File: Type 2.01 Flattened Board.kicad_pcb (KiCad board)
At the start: 4 copper layers, 170 x 170 mm, 74 parts, among them J1 Conn_02x03_Odd_Even, J4 Conn_02x03_Odd_Even, J5 Conn_02x03_Odd_Even, U1 74AHC74, U10 74AHC74, U11 74AHC157, U12 74AHC157, U13 74AHC04, U14 ATmega4809-PF, U15 74AHC04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

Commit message: More pcb layout changes
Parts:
- removed C33, C34: 0.1uF, Capacitor_SMD:C_0805_2012Metric_Pad1.18x1.45mm_HandSolder
- removed U12, U22: 74AHC157, Package_SO:SOIC-16_3.9x9.9mm_P1.27mm
- U11, U2, U6: value 74AHC157 -> 74AHC245; footprint Package_SO:SOIC-16_3.9x9.9mm_P1.27mm -> Package_SO:SOIC-20W_7.5x12.8mm_P1.27mm
- U3: value 74AHC157 -> 74AHC138
- moved C37 108.1 mm to (89.9, 116.7), turned to 90 degrees
- moved U5 99.8 mm to (82.1, 112.6), turned to -90 degrees
- moved C15 97.4 mm to (104.7, 120.6), turned to 0 degrees
- moved C19 88.5 mm to (196.0, 47.9), turned to 180 degrees
- moved U4 83.1 mm to (191.9, 55.7), turned to 0 degrees
- moved U11 80.4 mm to (108.7, 112.8), turned to 180 degrees
- moved C5 67.9 mm to (133.5, 125.7), turned to 90 degrees
- moved C4 48.4 mm to (63.8, 98.1)
- moved C3 42.5 mm to (114.7, 78.0), turned to 90 degrees
- moved C2 40.7 mm to (162.6, 81.5)
- moved U17 38.9 mm to (127.1, 123.9), turned to -90 degrees
- moved U2 28.7 mm to (158.5, 89.3)
- moved U6 23.1 mm to (145.3, 76.3), turned to 90 degrees
- moved U3 19.0 mm to (108.3, 76.2), turned to -90 degrees
- moved C14 11.5 mm to (137.5, 72.2), turned to -90 degrees
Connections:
- U11 pad 1: /i960/SEL0 -> VCC
- U11 pad 10: /i960.A26 -> GND
- U11 pad 11: /i960.A10 -> /GCM4.L7
- U11 pad 12: /i960/Q11 -> /GCM4.L6
- U11 pad 13: /i960.A27 -> /GCM4.L5
- U11 pad 14: /i960.A11 -> /GCM4.L4
- U11 pad 15: GND -> /GCM4.L3
- U11 pad 16: VCC -> /GCM4.L2
- U11 pad 2: /i960.A8 -> /i960.DT\~{R}
- U11 pad 3: /i960.A24 -> /i960.BURST_A1
- U11 pad 4: /i960/Q8 -> /i960.BURST_A2
- U11 pad 5: /i960.A9 -> /i960.BURST_A3
- U11 pad 6: /i960.A25 -> /i960.~{BE0}
- U11 pad 7: /i960/Q9 -> /i960.~{BE1}
- U11 pad 8: GND -> /i960/CTRL07/IN6
- U11 pad 9: /i960/Q10 -> /i960/CTRL07/IN7
- U18 pad 1: /i960/i960.~{DEV_EN0} -> /i960/i960.~{DEV_EN1}
- U18 pad 12: /i960.A15 -> /GCM4.L7
- U18 pad 13: /i960.A14 -> /GCM4.L6
- U18 pad 14: /i960.A13 -> /GCM4.L5
- U18 pad 15: /i960.A12 -> /GCM4.L4
- U18 pad 16: /i960.A11 -> /GCM4.L3
- U18 pad 17: /i960.A10 -> /GCM4.L2
- U18 pad 18: /i960.A9 -> /GCM4.L1
- U18 pad 19: /i960.A8 -> /GCM4.L0
- U19 pad 12: /i960.A7 -> /GCM4.L7
- U19 pad 13: /i960.A6 -> /GCM4.L6
- U19 pad 14: /i960.A5 -> /GCM4.L5
- U19 pad 15: /i960.A4 -> /GCM4.L4
- U19 pad 16: /i960.A3 -> /GCM4.L3
- U19 pad 17: /i960.A2 -> /GCM4.L2
- U19 pad 18: /i960.A1 -> /GCM4.L1
- U19 pad 19: /i960.A0 -> /GCM4.L0
- U2 pad 1: /i960/SEL0 -> VCC
- U2 pad 10: /i960.A22 -> GND
- U2 pad 11: /i960.A6 -> /GCM4.L7
- U2 pad 12: /i960/Q7 -> /GCM4.L6
- U2 pad 13: /i960.A23 -> /GCM4.L5
- U2 pad 14: /i960.A7 -> /GCM4.L4
- U2 pad 15: GND -> /GCM4.L3
- U2 pad 16: VCC -> /GCM4.L2
- U2 pad 2: /i960.A4 -> /i960.A24
- U2 pad 3: /i960.A20 -> /i960.A25
- U2 pad 4: /i960/Q5 -> /i960.A26
- U2 pad 5: /i960.A5 -> /i960.A27
- U2 pad 6: /i960.A21 -> /i960.A28
- U2 pad 7: /i960/Q6 -> /i960.A29
- U2 pad 8: GND -> /i960.A30
- U2 pad 9: /i960/Q4 -> /i960.A31
- U3 pad 1: /i960/SEL0 -> /i960/GCM4.LA0
- U3 pad 10: /i960.A18 -> /i960/i960.~{DEV_EN5}
- U3 pad 11: /i960.A2 -> /i960/i960.~{DEV_EN4}
- U3 pad 12: /i960/Q3 -> /i960/i960.~{DEV_EN3}
- U3 pad 13: /i960.A19 -> /i960/i960.~{DEV_EN2}
- U3 pad 14: /i960.A3 -> /i960/i960.~{DEV_EN1}
- U3 pad 15: GND -> /i960/i960.~{DEV_EN0}
- U3 pad 2: /i960.A0 -> /i960/GCM4.LA1
- U3 pad 3: /i960.A16 -> /i960/GCM4.LA2
- U3 pad 4: /i960/Q0 -> /i960/GCM4.~{EN}
- U3 pad 5: /i960.A1 -> GND
- U3 pad 6: /i960.A17 -> VCC
- U3 pad 7: /i960/Q1 -> /i960/i960.~{DEV_EN7}
- U3 pad 9: /i960/Q2 -> /i960/i960.~{DEV_EN6}
- U6 pad 1: /i960/SEL0 -> VCC
- U6 pad 10: /i960.A30 -> GND
- U6 pad 11: /i960.A14 -> /GCM4.L7
- U6 pad 12: /i960/Q15 -> /GCM4.L6
- U6 pad 13: /i960.A31 -> /GCM4.L5
- U6 pad 14: /i960.A15 -> /GCM4.L4
- U6 pad 15: GND -> /GCM4.L3
- U6 pad 16: VCC -> /GCM4.L2
- U6 pad 2: /i960.A12 -> /i960.A16
- U6 pad 3: /i960.A28 -> /i960.A17
- U6 pad 4: /i960/Q13 -> /i960.A18
- U6 pad 5: /i960.A13 -> /i960.A19
- U6 pad 6: /i960.A29 -> /i960.A20
- U6 pad 7: /i960/Q14 -> /i960.A21
- U6 pad 8: GND -> /i960.A22
- U6 pad 9: /i960/Q12 -> /i960.A23

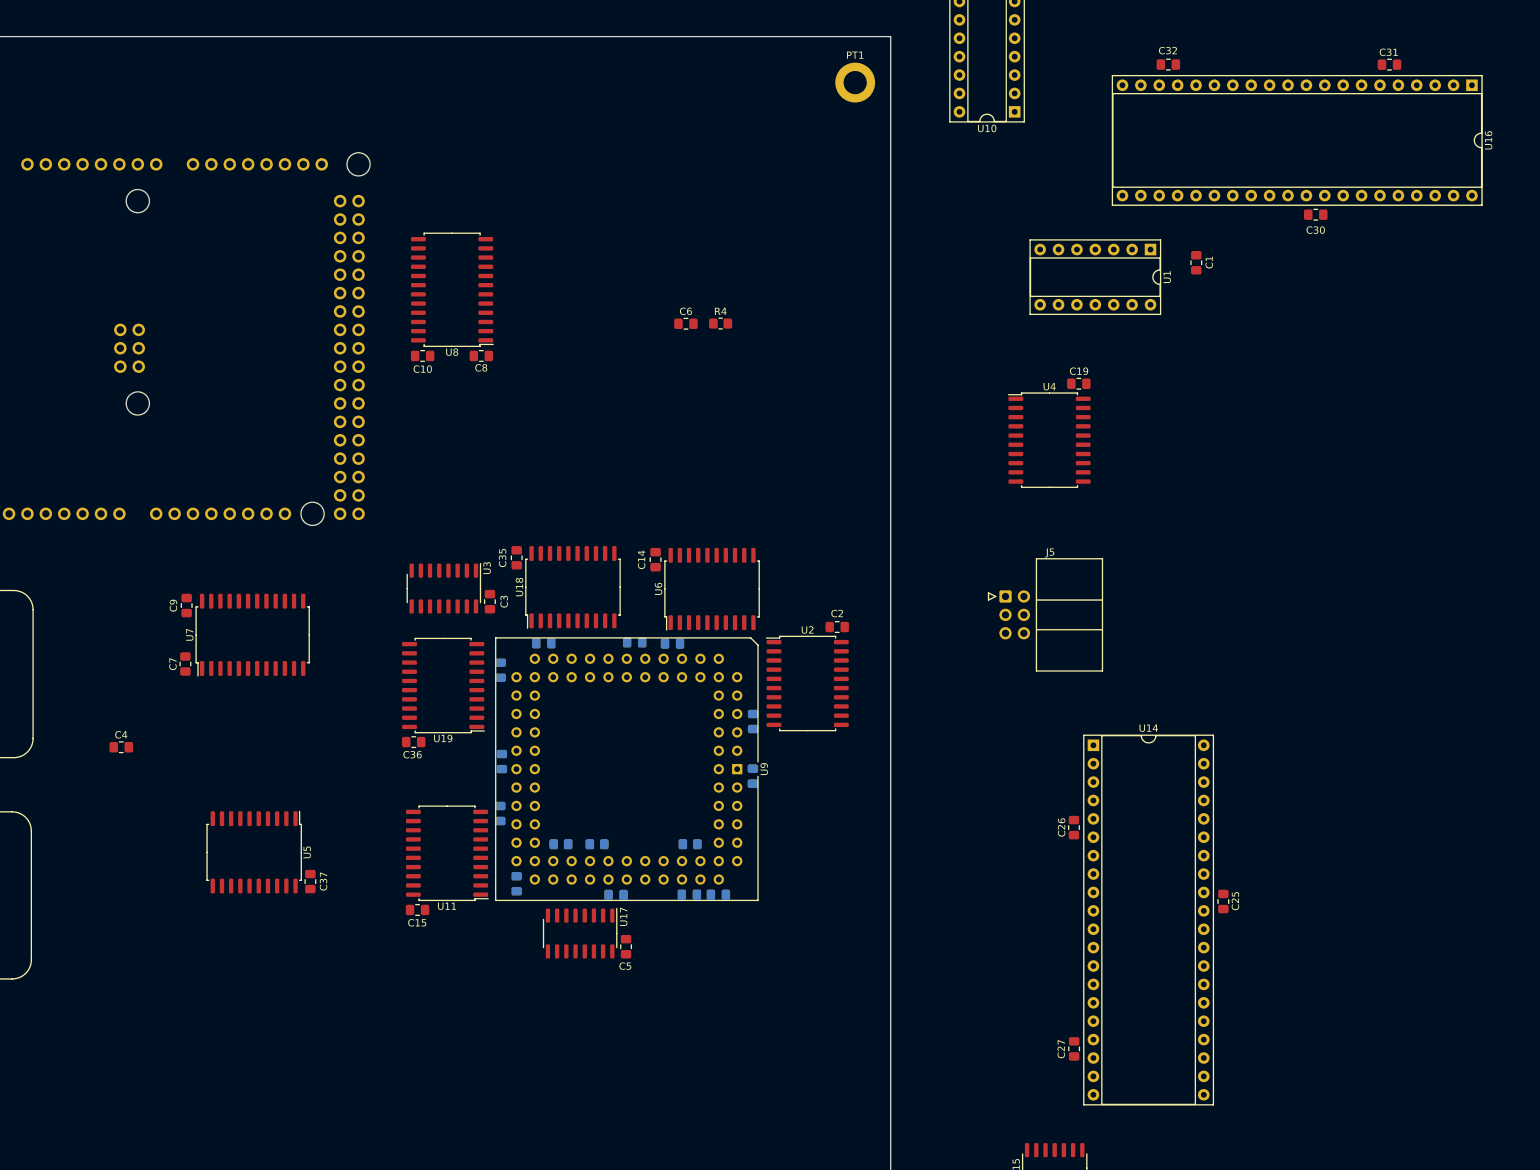
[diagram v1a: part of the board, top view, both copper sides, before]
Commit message: More routing + drop attaching ~{AS} to anything
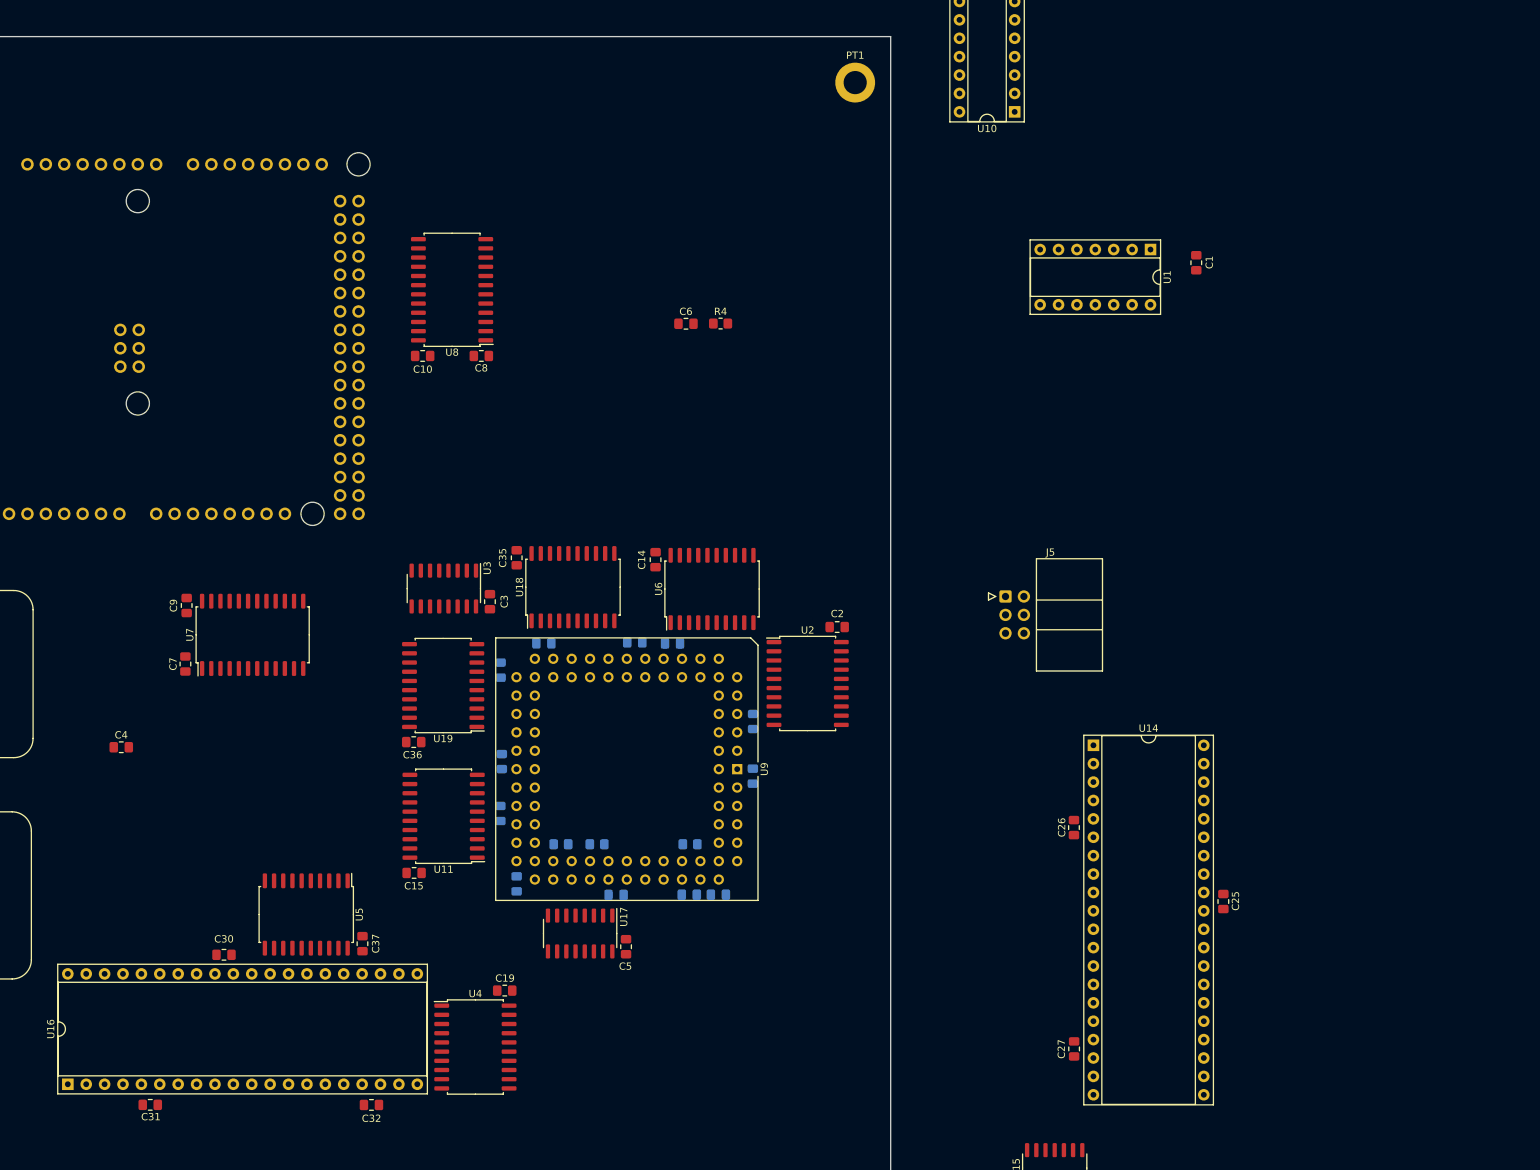
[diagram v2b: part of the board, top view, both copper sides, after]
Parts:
- moved U16 238.0 mm to (56.4, 144.7), turned to 90 degrees
- moved C31 223.4 mm to (67.8, 147.5), turned to 0 degrees
- moved C30 182.1 mm to (77.9, 126.8), turned to 180 degrees
- moved C32 181.0 mm to (98.3, 147.5), turned to 0 degrees
- moved U4 115.4 mm to (112.7, 139.5)
- moved C19 115.4 mm to (116.7, 131.7)
- moved U5 11.2 mm to (89.3, 121.2)
- moved C37 11.2 mm to (97.1, 125.3)
- moved U11 5.14 mm to (108.3, 107.7)
- moved C15 5.14 mm to (104.2, 115.5)

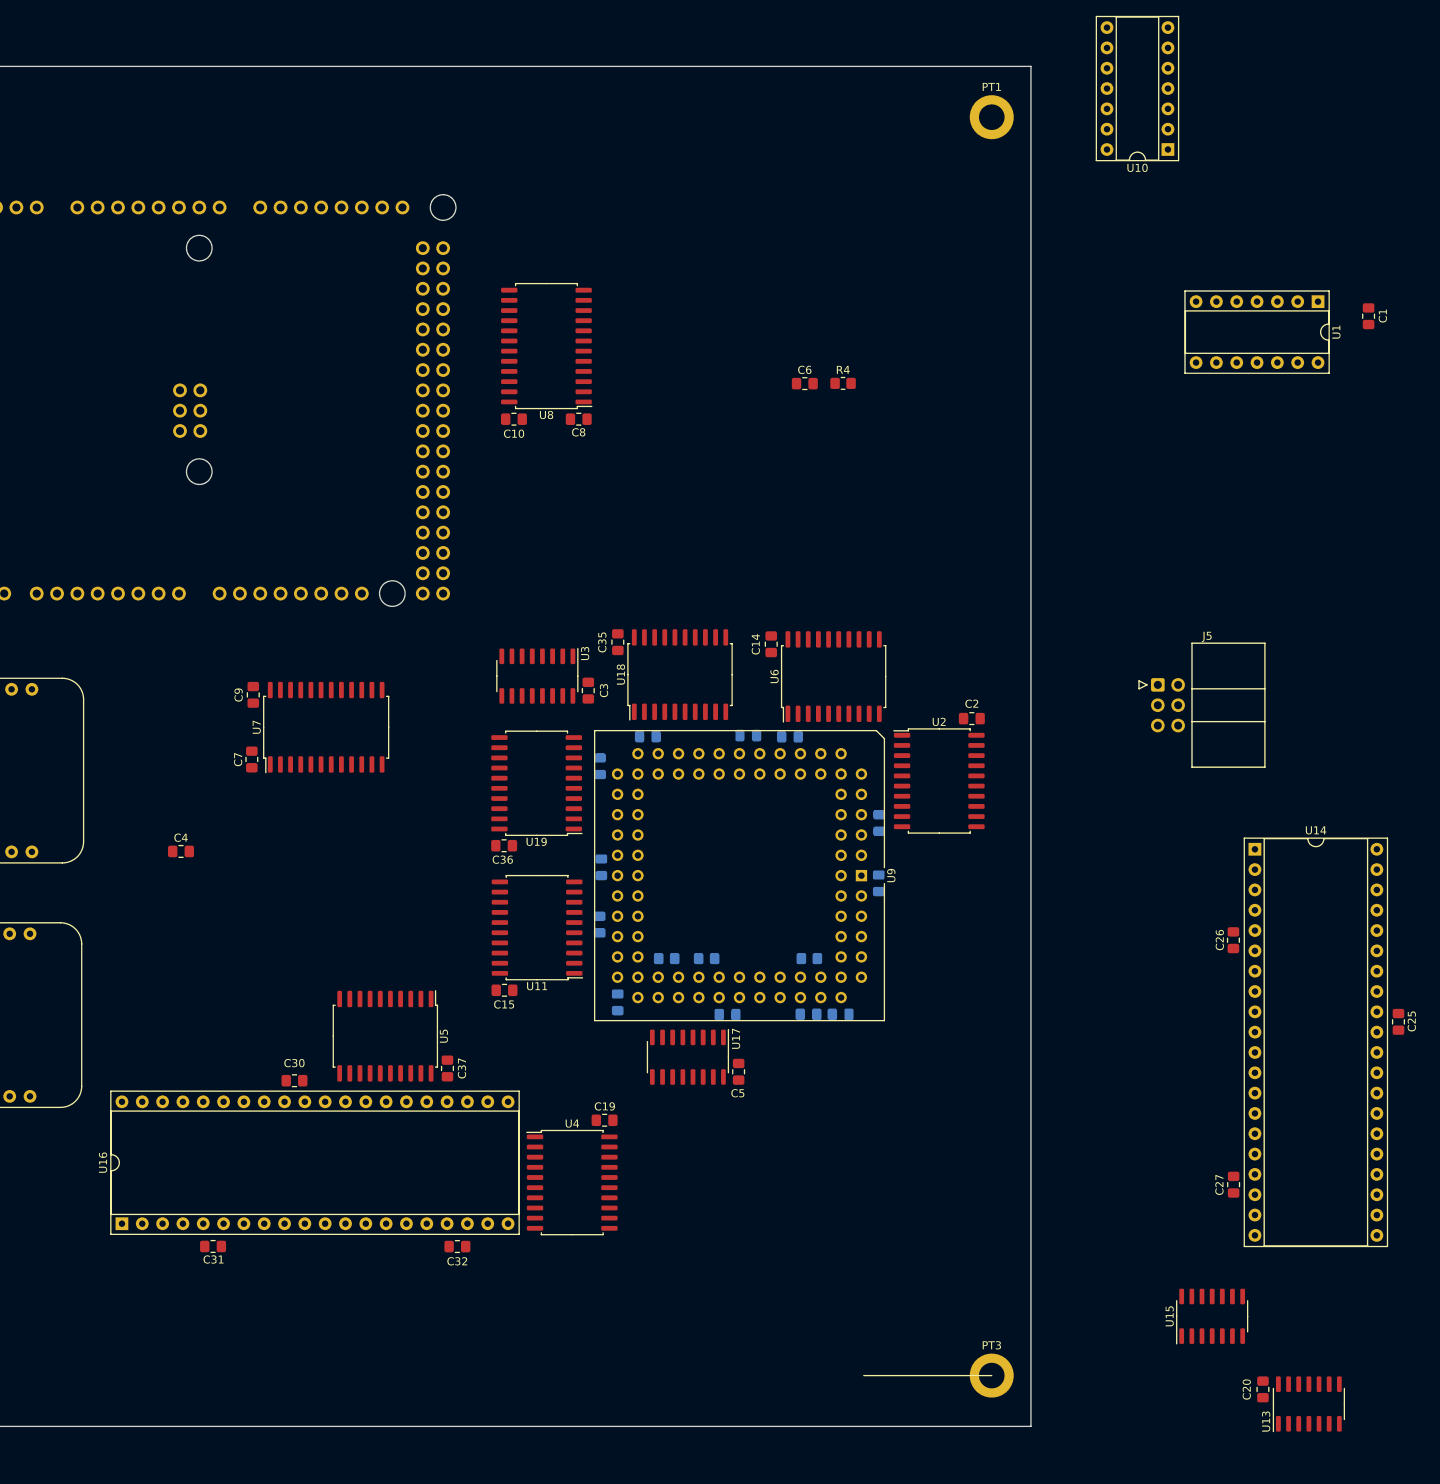
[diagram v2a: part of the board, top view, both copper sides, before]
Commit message: Drop an AHC74 and two resistor packs
Add an AHC174 in its place. This is for the edge detector. It should now
be far simpler to route this compared to an AHC74
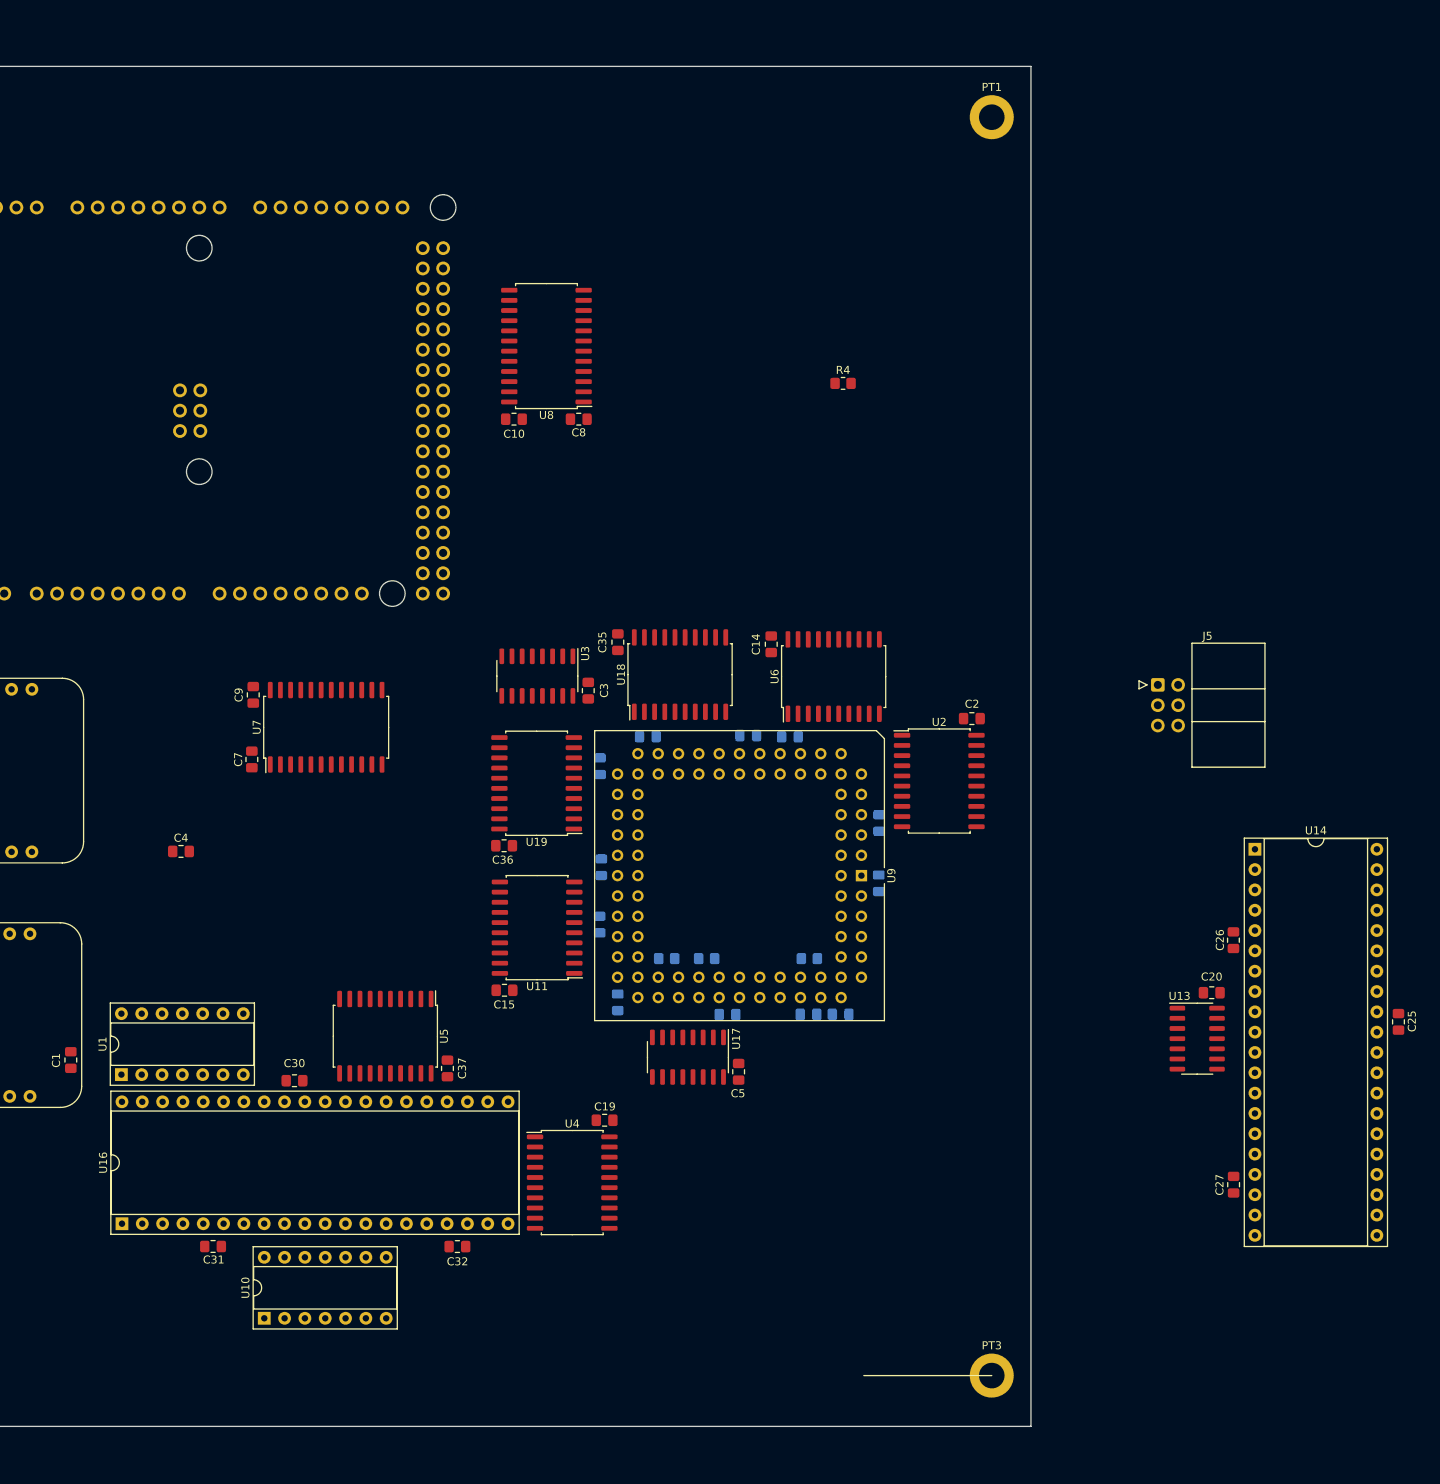
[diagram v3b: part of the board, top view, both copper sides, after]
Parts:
- removed C6: 0.1uF, Capacitor_SMD:C_0805_2012Metric_Pad1.18x1.45mm_HandSolder
- removed U15: 74AHC04, Package_SO:SOIC-14_3.9x8.7mm_P1.27mm
- moved C1 187.0 mm to (50.0, 124.2), turned to -90 degrees
- moved U10 184.7 mm to (74.2, 156.5), turned to 90 degrees
- moved U1 178.1 mm to (56.3, 126.0), turned to 90 degrees
- moved C20 50.0 mm to (192.6, 115.8), turned to 180 degrees
- moved U13 47.8 mm to (190.8, 121.5), turned to 0 degrees
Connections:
- RN1 pad 7: /i960/~{RUN_PIC} -> /i960/~{CLK_READY}
- U13 pad 10: Net-(U14-Pad29) -> (no net)
- U13 pad 11: /i960/~{RUN_PIC} -> (no net)
- U13 pad 12: /i960/i960.HOLD -> (no net)
- U13 pad 13: /GCM4.HOLD -> (no net)
- U14 pad 29: Net-(U14-Pad29) -> /i960/5V_~{RESET}
- U14 pad 39: /i960/i960.~{BOOT_SUCCESSFUL} -> /i960/PIC.PA6
- U14 pad 40: /i960/PIC.PA7 -> /i960/~{CLK_READY}
- U16 pad 15: /i960/~{RUN_PIC} -> /i960/~{CLK_READY}
- U16 pad 28: /i960/i960.~{AS} -> /i960.~{DEN}
- U16 pad 33: /i960.~{DEN} -> /i960/ME.PA0
- U4 pad 11: /GCM4.CLK -> unconnected-(U4-Pad11)
- U4 pad 12: /GCM4.CLK2 -> unconnected-(U4-Pad12)
- U4 pad 13: /GCM4.USART_PIC_RX -> /GCM4.HLDA
- U4 pad 14: unconnected-(U4-Pad14) -> /GCM4.USART_PIC_RX
- U4 pad 6: unconnected-(U4-Pad6) -> /i960/PIC.TX
- U4 pad 7: /i960/PIC.TX -> /i960/i960.HLDA
- U4 pad 8: /i960.CLK2 -> unconnected-(U4-Pad8)
- U4 pad 9: /i960.CLK -> unconnected-(U4-Pad9)
- U5 pad 13: unconnected-(U5-Pad13) -> /i960/i960.HOLD
- U5 pad 7: unconnected-(U5-Pad7) -> /GCM4.HOLD
